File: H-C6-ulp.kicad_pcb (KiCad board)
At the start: 4 copper layers, 50.3 x 33 mm, 60 parts, among them J1 USB_C_Receptacle_USB2.0, J2 AFC24-S24FIC-00, J3 SM02B-SRSS-TB, Q1 Si1308, Q2 Si2301CDS, U1 ESP32-C6, U2 SGM6029CYG/TR, U3 TP4057-42-SOT26-R, X1 Crystal 40 Mhz 10ppm, Y1 RV-3032-C7

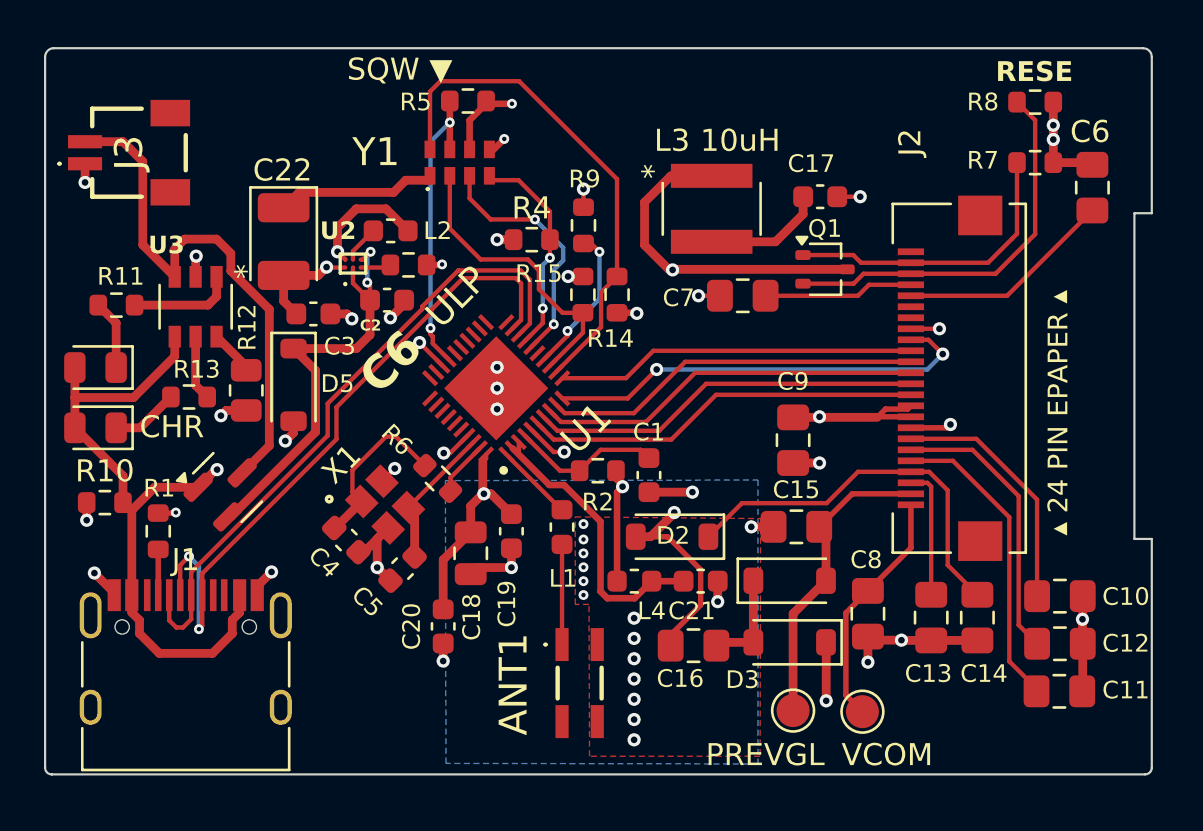
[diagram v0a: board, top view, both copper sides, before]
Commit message: Add QWIIC I2c connector
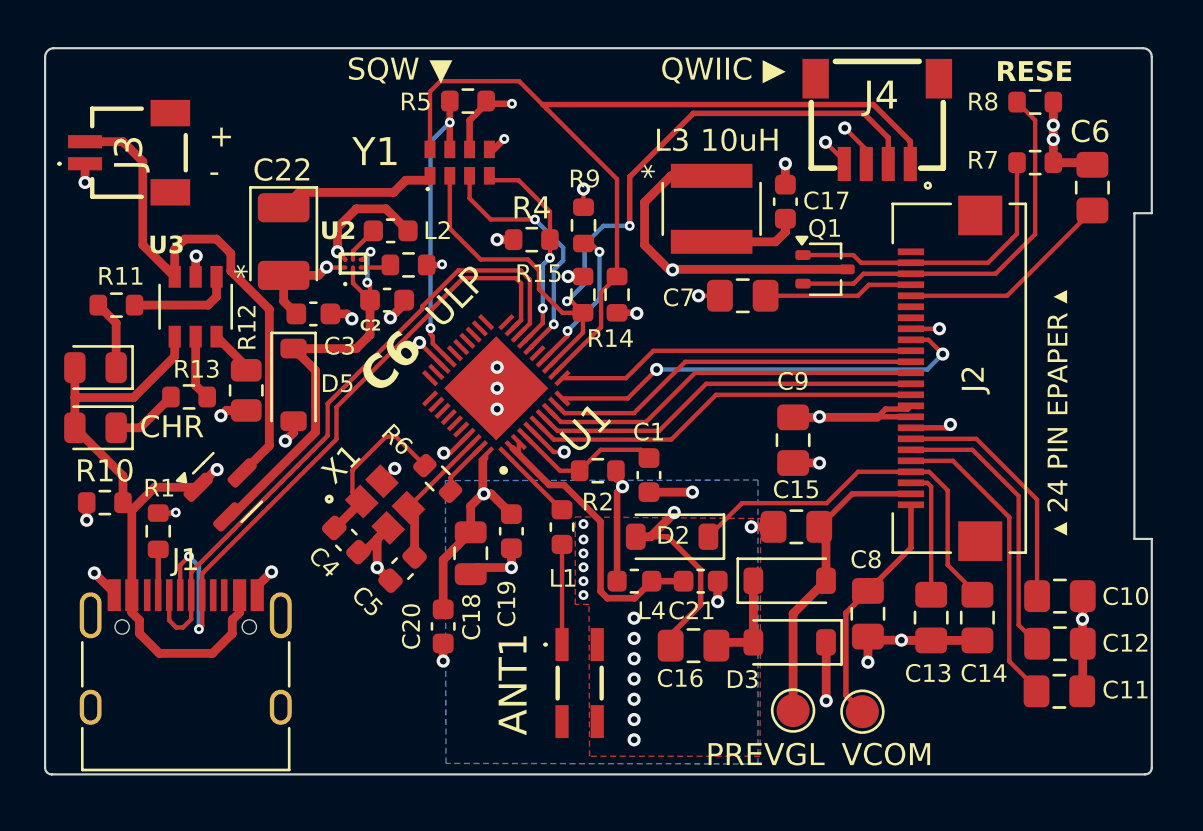
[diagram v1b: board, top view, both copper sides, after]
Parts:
- added J4: SM04B-SRSS-TB_LF__SN_, footprints:QWIIC_SM04B-SRSS-TB_LFSN_, F.Cu at (159.0, 48.2)
- moved C17 1.60 mm to (151.8, 54.6), turned to -90 degrees
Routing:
- net /SDA: track 13.4 -> 36.4 mm, vias 0 -> 2
- net /SCL: track 23.3 -> 41.7 mm
- net VDD33: track 40.3 -> 42.0 mm, vias 13 -> 14
- net +3V3: track 5.47 -> 4.14 mm
- net GND: track 52.9 -> 53.9 mm, vias 45 -> 46
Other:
- board text added: "+ -"
- board text added: "QWIIC ▶"

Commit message: Rev 1.0 is quite ready for last review @bitbank2
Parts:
- added H1: MountingHole, MountingHole:MountingHole_2.2mm_M2, F.Cu at (120.9, 50.2)
- added H2: MountingHole, MountingHole:MountingHole_2.2mm_M2, F.Cu at (166.0, 50.2)
- added H3: MountingHole, MountingHole:MountingHole_2.2mm_M2, F.Cu at (132.6, 78.0)
- added H4: MountingHole, MountingHole:MountingHole_2.2mm_M2, F.Cu at (166.0, 78.0)
- added TP1: VGH, TestPoint:TestPoint_Pad_D1.5mm, F.Cu at (158.2, 77.7)
- J3: value SM02B-SRSS-TB -> SM02B-SRSS-TB(LF)(SN)
- moved C22 5.80 mm to (132.6, 51.8), turned to 90 degrees
- moved J3 4.53 mm to (126.8, 51.7), turned to 0 degrees
- moved C11 2.92 mm to (161.6, 77.9)
- moved C9 1.47 mm to (152.3, 66.9), turned to 0 degrees
- moved R8 1.28 mm to (161.9, 50.1)
- moved C6 0.91 mm to (165.2, 54.6), turned to 180 degrees
- moved R7 0.72 mm to (162.5, 52.8)
- moved C12 0.25 mm to (164.5, 74.5)
- moved C10 0.18 mm to (164.5, 72.4)
- moved TP2 0.16 mm to (155.2, 77.7)
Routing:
- net PREVGH: track 17.8 -> 25.8 mm
- net VDD_RTC: track 7.17 -> 3.13 mm
- net GND: track 53.9 -> 57.8 mm, vias 46 -> 48
- net /USB_D+: track 31.3 -> 27.5 mm, vias 2 -> 0
- net VDD33: track 42.0 -> 45.7 mm, vias 14 -> 15
- net Net-(C11-Pad2): track 13.9 -> 15.2 mm
- net VBAT: track 24.3 -> 23.3 mm
- net /USB_D-: track 29.4 -> 28.4 mm
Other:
- board text added: "+"
- board text added: "0 1 2 3 4 5 6 7"
- board text added: "VGH"
- board text added: "VGL"
- board text added: "github.com/martinberlin/H-C6-ulp"
- board text added: "r1.0"
- board text removed: "+ -"
- board text removed: "PREVGL"

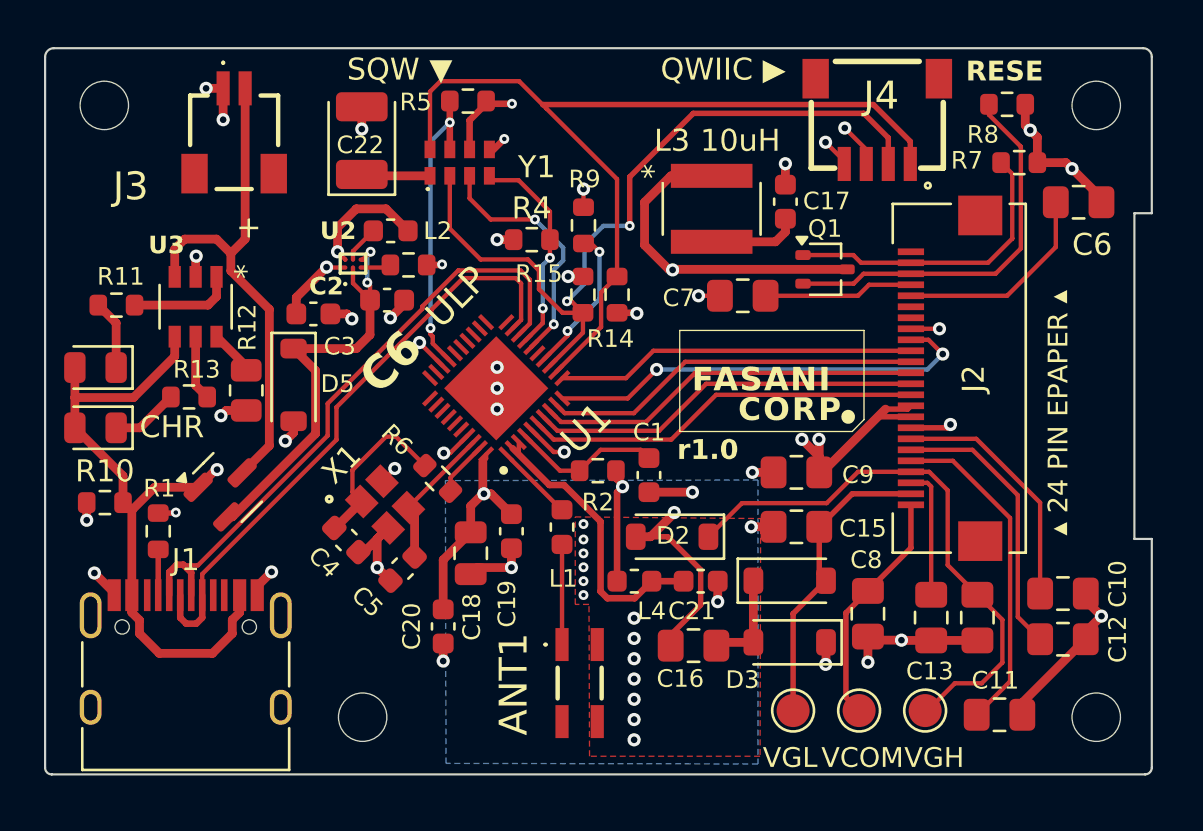
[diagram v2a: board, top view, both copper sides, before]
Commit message: Move mounting H out of display area
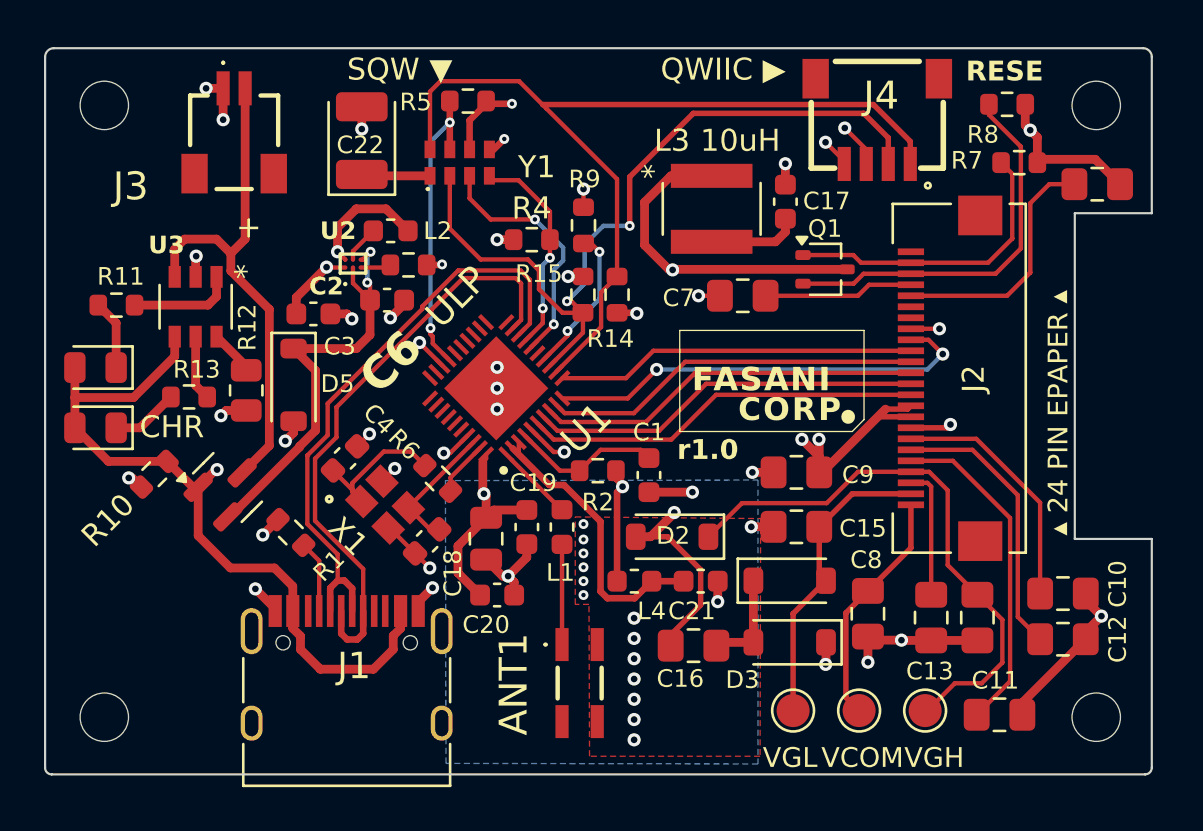
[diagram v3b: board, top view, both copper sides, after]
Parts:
- moved H3 11.7 mm to (120.9, 78.0)
- moved J1 7.35 mm to (131.9, 77.2)
- moved R1 6.03 mm to (129.4, 69.6), turned to 135 degrees
- moved C4 3.71 mm to (131.8, 66.2), turned to -135 degrees
- moved C20 2.83 mm to (138.8, 72.5), turned to 180 degrees
- moved R10 2.59 mm to (123.2, 67.0), turned to 45 degrees
- moved C5 1.67 mm to (135.6, 70.0)
- moved C6 1.18 mm to (166.0, 53.8)
- moved C18 0.96 mm to (138.2, 69.9)
- moved C19 0.73 mm to (140.1, 69.4)
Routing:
- net VBUS: track 35.7 -> 38.9 mm
- net Net-(C6-Pad2): track 9.54 -> 11.4 mm
- net /USB_D-: track 28.4 -> 27.0 mm
- net Net-(C4-Pad2): track 7.81 -> 6.40 mm
- net Net-(J1-CC1): track 2.08 -> 3.28 mm
- net Net-(U1-XTAL_N): track 6.55 -> 6.02 mm
- net GND: track 57.8 -> 57.7 mm, vias 48 -> 47
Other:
- outline, holes or cut-outs redrawn
- board text added: "6.5"

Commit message: Add BOOT & RST switches
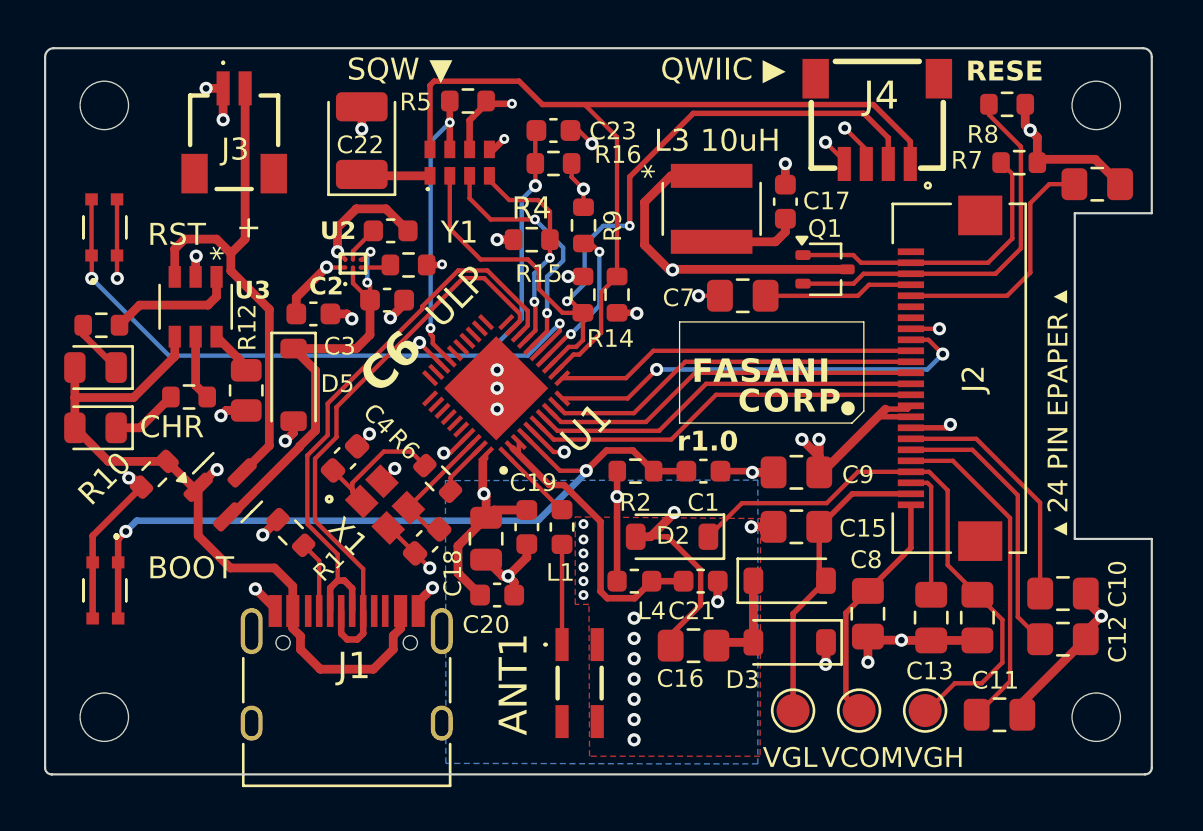
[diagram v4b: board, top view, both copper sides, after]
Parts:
- added C23: 22pF, Capacitor_SMD:C_0603_1608Metric, F.Cu at (141.3, 51.3)
- added R16: 10k, Resistor_SMD:R_0603_1608Metric, F.Cu at (141.3, 52.8)
- added SW1: SW_Push_Dual, footprints:switch_SKSVCCE010, F.Cu at (121.0, 72.2)
- added SW2: SW_Push_Dual, footprints:switch_SKSVCCE010, F.Cu at (120.9, 55.7)
- moved C1 2.48 mm to (148.1, 66.8), turned to 180 degrees
- moved R2 1.71 mm to (145.0, 66.8)
- moved R11 1.14 mm to (120.8, 60.2)
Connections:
- C1 pad 2: Net-(U1-CHIP_PU) -> ENABLE
- R2 pad 1: VDD33 -> ENABLE
- R2 pad 2: Net-(U1-CHIP_PU) -> VDD33
- U1 pad 15: unconnected-(U1-GPIO9-Pad15) -> BOOT
- U1 pad 4: Net-(U1-CHIP_PU) -> ENABLE
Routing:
- net BOOT: track 0.00 -> 39.9 mm, vias 0 -> 3
- net ENABLE: track 0.00 -> 34.7 mm, vias 0 -> 2
- net GND: track 57.7 -> 68.9 mm, vias 47 -> 48
- net Net-(U1-CHIP_PU): track 6.84 -> 0.00 mm
- net VDD33: track 45.7 -> 46.8 mm
- net Net-(U3-*CHRG): track 4.78 -> 5.85 mm
- net /USB_D-: track 27.0 -> 26.0 mm
- net /USB_D+: track 27.0 -> 26.1 mm
- net /SCL: track 41.7 -> 41.0 mm
- net Net-(D4-K): track 3.17 -> 2.54 mm
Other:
- board text added: "BOOT"
- board text added: "RST"

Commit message: 3 buttons, a bit risky routing
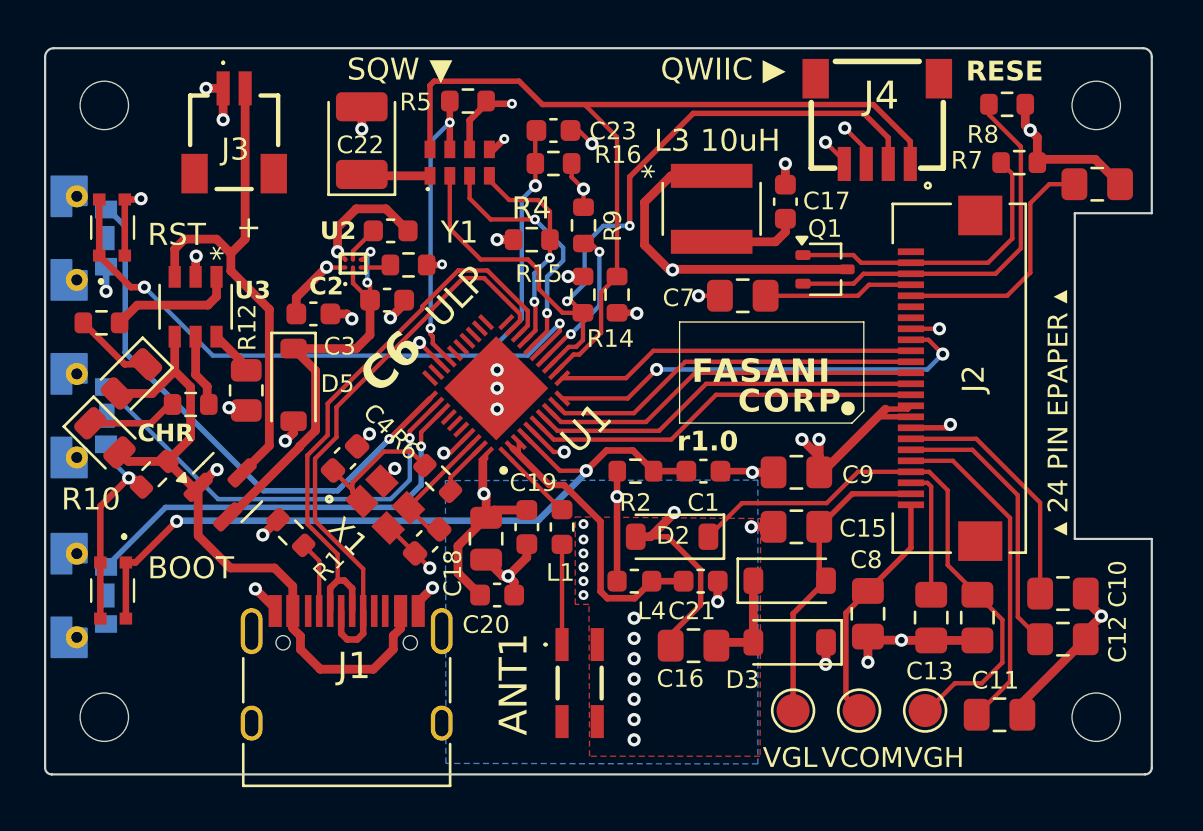
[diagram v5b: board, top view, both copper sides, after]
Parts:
- added U4: K2-1806SQ-A2DW-04, footprints:KEY-SMD_K2-1806SQ-A3DW-04, B.Cu at (120.2, 56.2)
- added U5: K2-1806SQ-A2DW-04, footprints:KEY-SMD_K2-1806SQ-A3DW-04, B.Cu at (120.2, 64.3)
- added U6: K2-1806SQ-A2DW-04, footprints:KEY-SMD_K2-1806SQ-A3DW-04, B.Cu at (120.2, 72.5)
- moved D4 1.71 mm to (122.1, 62.6), turned to -135 degrees
- moved D6 0.63 mm to (120.9, 65.3), turned to -45 degrees
- moved SW1 0.35 mm to (121.3, 72.2)
- moved SW2 0.35 mm to (121.2, 55.8)
- moved R13 0.35 mm to (124.8, 63.8)
- moved R11 0.11 mm to (120.8, 60.1)
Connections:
- U1 pad 31: unconnected-(U1-GPIO18/SDIO_CMD/FSPICS2-Pad31) -> SW18
- U1 pad 32: unconnected-(U1-GPIO19/SDIO_CLK/FSPICS3-Pad32) -> SW19
- U1 pad 33: unconnected-(U1-GPIO20/SDIO_DATA0/FSPICS4-Pad33) -> SW20
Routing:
- net SW18: track 0.00 -> 25.1 mm, vias 0 -> 1
- net SW19: track 0.00 -> 20.2 mm, vias 0 -> 1
- net SW20: track 0.00 -> 19.6 mm, vias 0 -> 1
- net GND: track 68.9 -> 71.3 mm, vias 48 -> 49
- net VBUS: track 38.9 -> 36.9 mm
- net Net-(D4-K): track 2.54 -> 3.63 mm
- net Net-(D6-K): track 3.07 -> 4.09 mm
- net ENABLE: track 34.7 -> 33.7 mm
- net BOOT: track 39.9 -> 38.9 mm

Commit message: Add Readme
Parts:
- moved U5 47.0 mm to (166.5, 72.5), turned to 90 degrees
- moved D4 1.80 mm to (120.3, 62.5), turned to 0 degrees
- moved D6 0.63 mm to (120.3, 65.5), turned to 0 degrees
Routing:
- net SW19: track 20.2 -> 36.5 mm
- net Net-(D6-K): track 4.09 -> 7.93 mm
- net VBUS: track 36.9 -> 38.1 mm
- net Net-(D4-K): track 3.63 -> 2.62 mm
- net GND: track 71.3 -> 71.8 mm
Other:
- outline, holes or cut-outs redrawn
- board text added: "18"
- board text added: "19"
- board text added: "20"
- board text added: "READY"
- board text added: "Rev 1.0"
- board text removed: "6.5"
